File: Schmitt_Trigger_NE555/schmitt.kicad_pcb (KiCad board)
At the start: 2 copper layers, 152.3 x 101.6 mm, 11 parts, among them J1 O/P, J2 GND, J3 VCC, J4 GND, J5 I/P, J6 GND, U1 LM555N

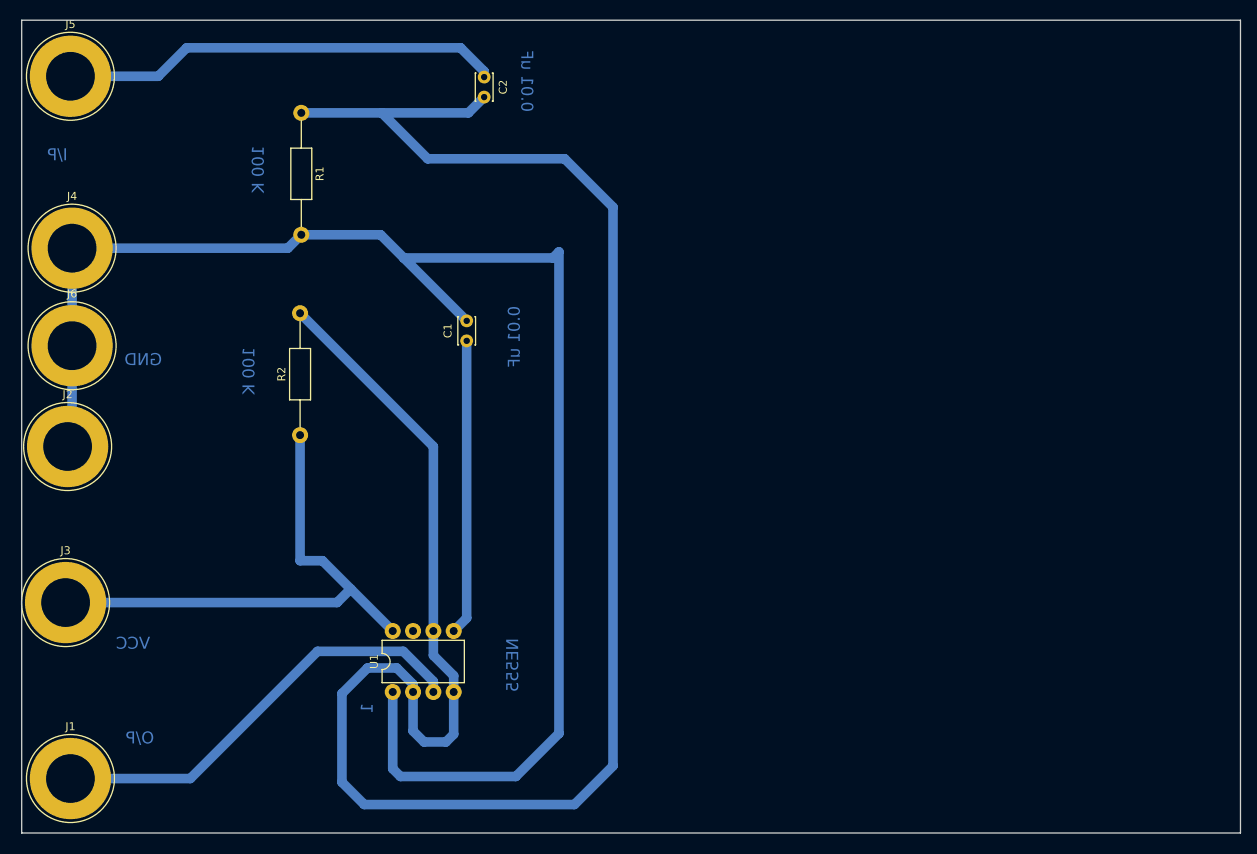
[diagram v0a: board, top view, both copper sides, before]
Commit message: Added V to I Converter
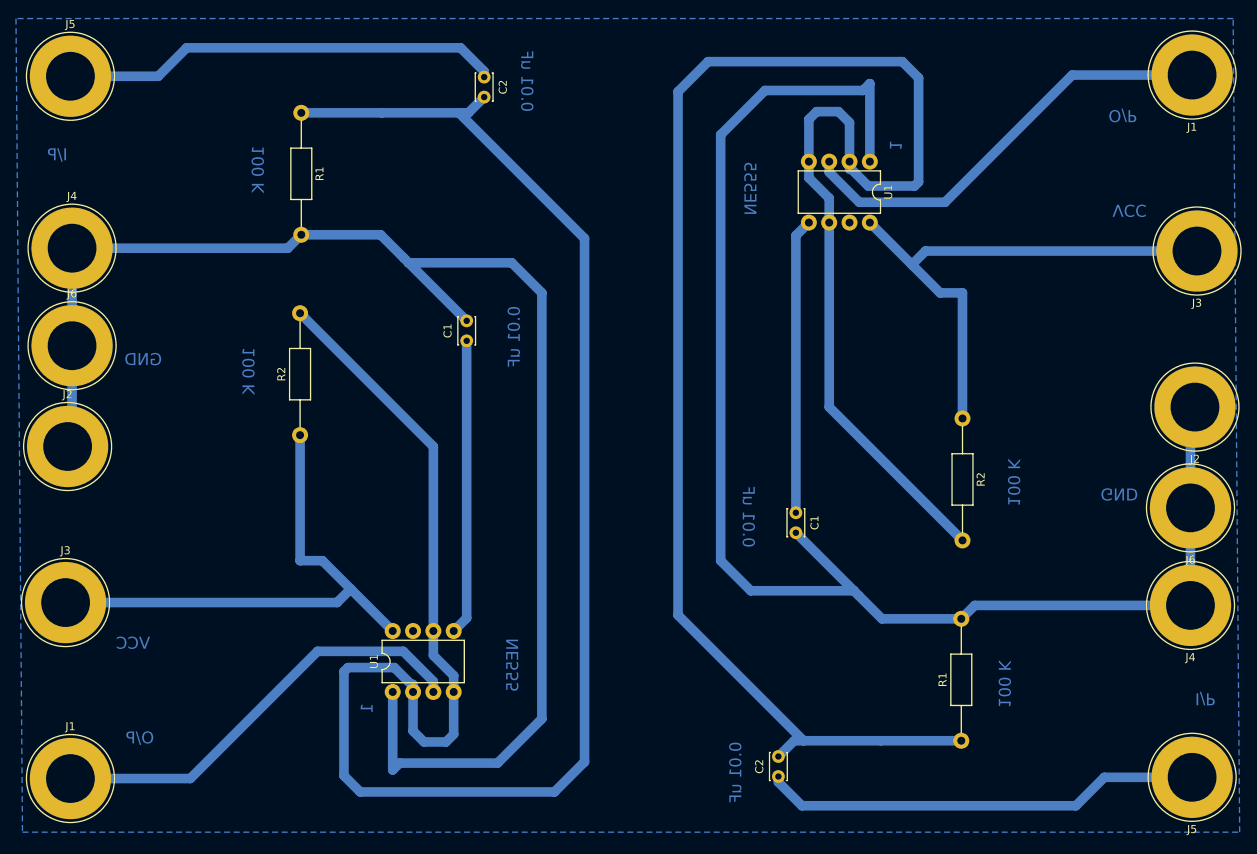
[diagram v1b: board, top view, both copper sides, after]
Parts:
- added C1: 0.01uF, Capacitors_THT:C_Disc_D3.4mm_W2.1mm_P2.50mm, F.Cu at (134.4, 91.8)
- added C2: 0.01uF, Capacitors_THT:C_Disc_D3.4mm_W2.1mm_P2.50mm, F.Cu at (132.2, 124.8)
- added J1: O/P, Connectors:Banana_Jack_1Pin, F.Cu at (183.9, 37.1)
- added J2: GND, Connectors:Banana_Jack_1Pin, F.Cu at (184.3, 78.6)
- added J3: VCC, Connectors:Banana_Jack_1Pin, F.Cu at (184.5, 59.1)
- added J4: GND, Connectors:Banana_Jack_1Pin, F.Cu at (183.7, 103.4)
- added J5: I/P, Connectors:Banana_Jack_1Pin, F.Cu at (183.9, 124.9)
- added J6: GND, Connectors:Banana_Jack_1Pin, F.Cu at (183.7, 91.2)
- added R1: 100k, Resistors_THT:R_Axial_DIN0207_L6.3mm_D2.5mm_P15.24mm_Horizontal, F.Cu at (155.0, 120.3)
- added R2: 100K, Resistors_THT:R_Axial_DIN0207_L6.3mm_D2.5mm_P15.24mm_Horizontal, F.Cu at (155.2, 80.0)
- added U1: LM555N, Housings_DIP:DIP-8_W7.62mm, F.Cu at (143.6, 47.9)
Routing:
- net Net-(C2-Pad2): track 260.0 -> 481.7 mm
- net GND: track 192.9 -> 364.9 mm
- net Net-(J3-Pad1): track 67.3 -> 134.5 mm
- net Net-(C2-Pad1): track 55.3 -> 110.5 mm
- net Net-(J1-Pad1): track 55.2 -> 110.4 mm
- net Net-(C1-Pad1): track 36.9 -> 73.9 mm
- added copper zone on B.Cu, net (none)
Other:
- board outline removed
